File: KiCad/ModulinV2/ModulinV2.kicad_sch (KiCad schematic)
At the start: 13 parts, among them IC1 TL074HIDR, J1 NRJ4HF-1

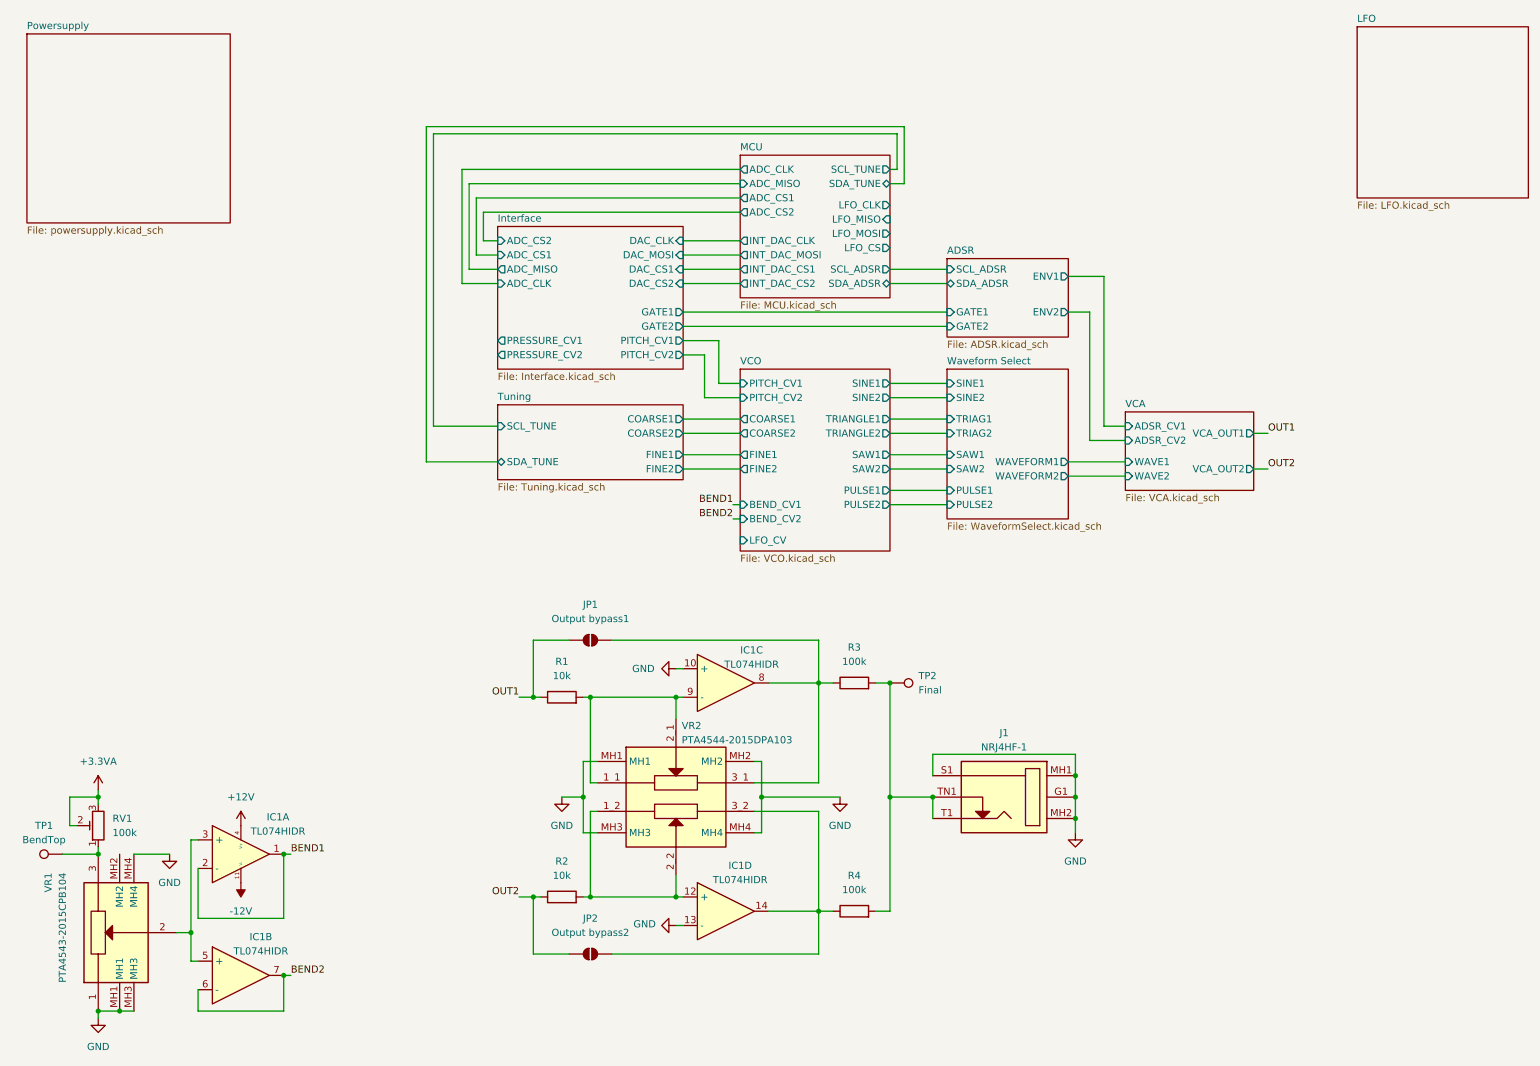
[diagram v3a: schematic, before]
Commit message: Made LFO and VCF schematics in addition to making a better reference voltage supply
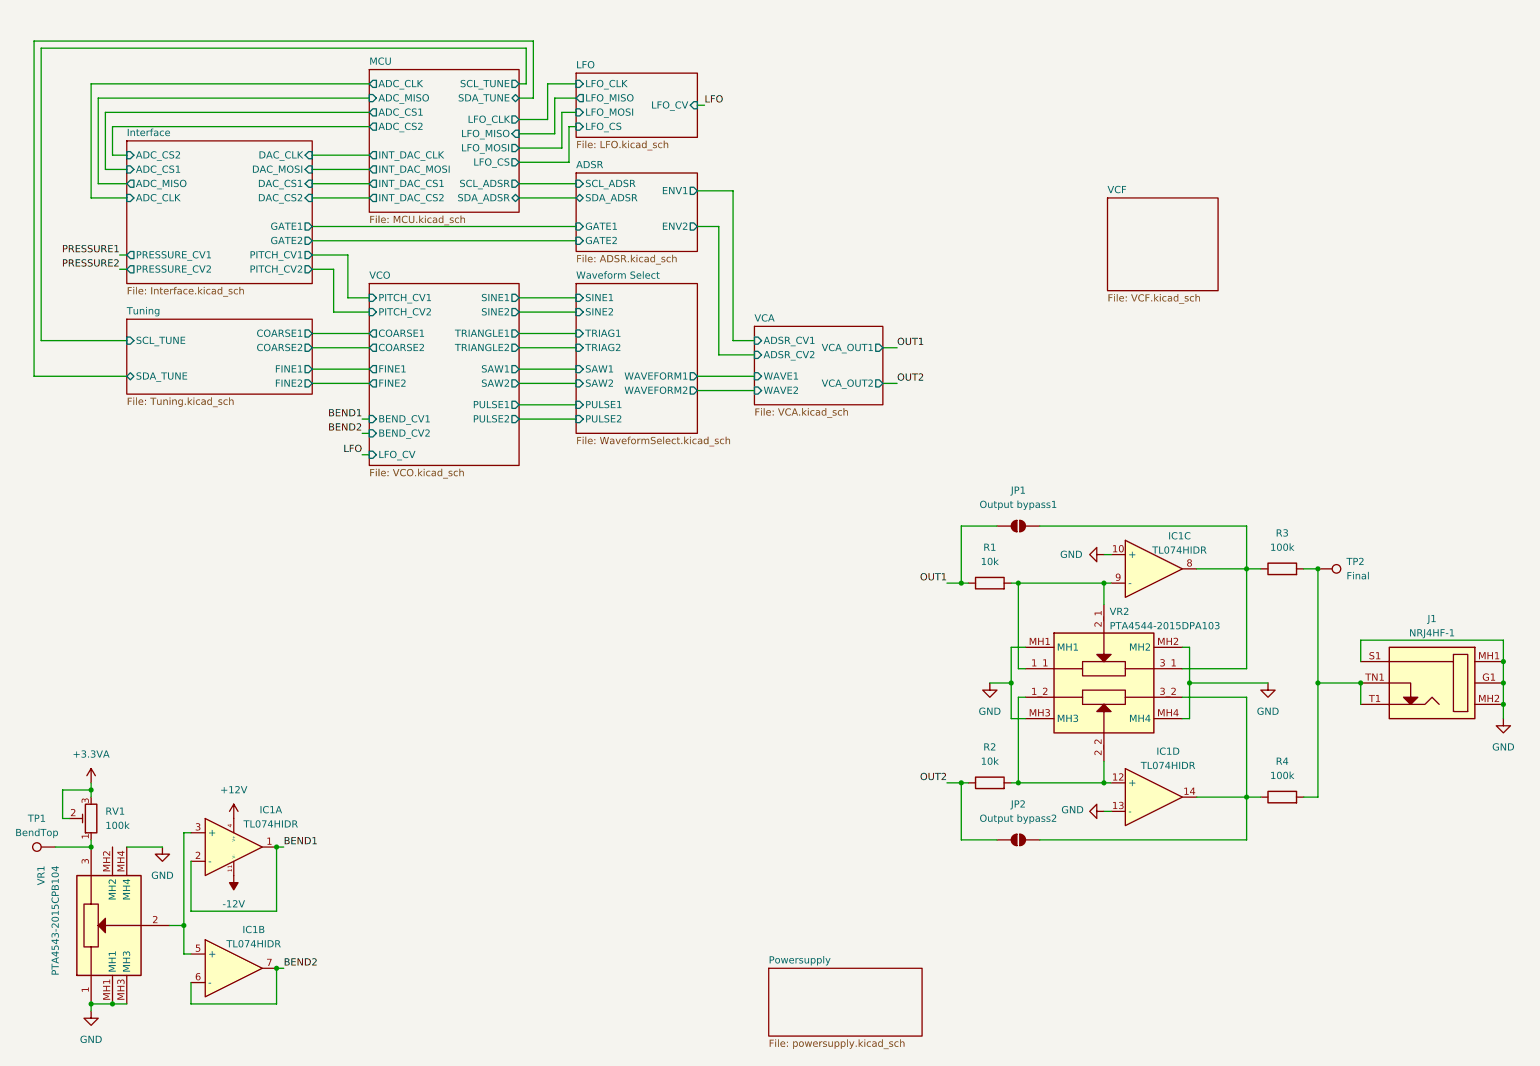
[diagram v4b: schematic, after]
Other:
- added sheet VCF (VCF.kicad_sch)
- sheet LFO ports: added LFO_CLK, LFO_CS, LFO_CV, LFO_MISO, LFO_MOSI; removed none
- moved on the sheet: IC1A, IC1B, IC1C, IC1D, J1, JP1, JP2, R1, R2, R3, R4, RV1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

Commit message: Finished Schematic, started on PCB
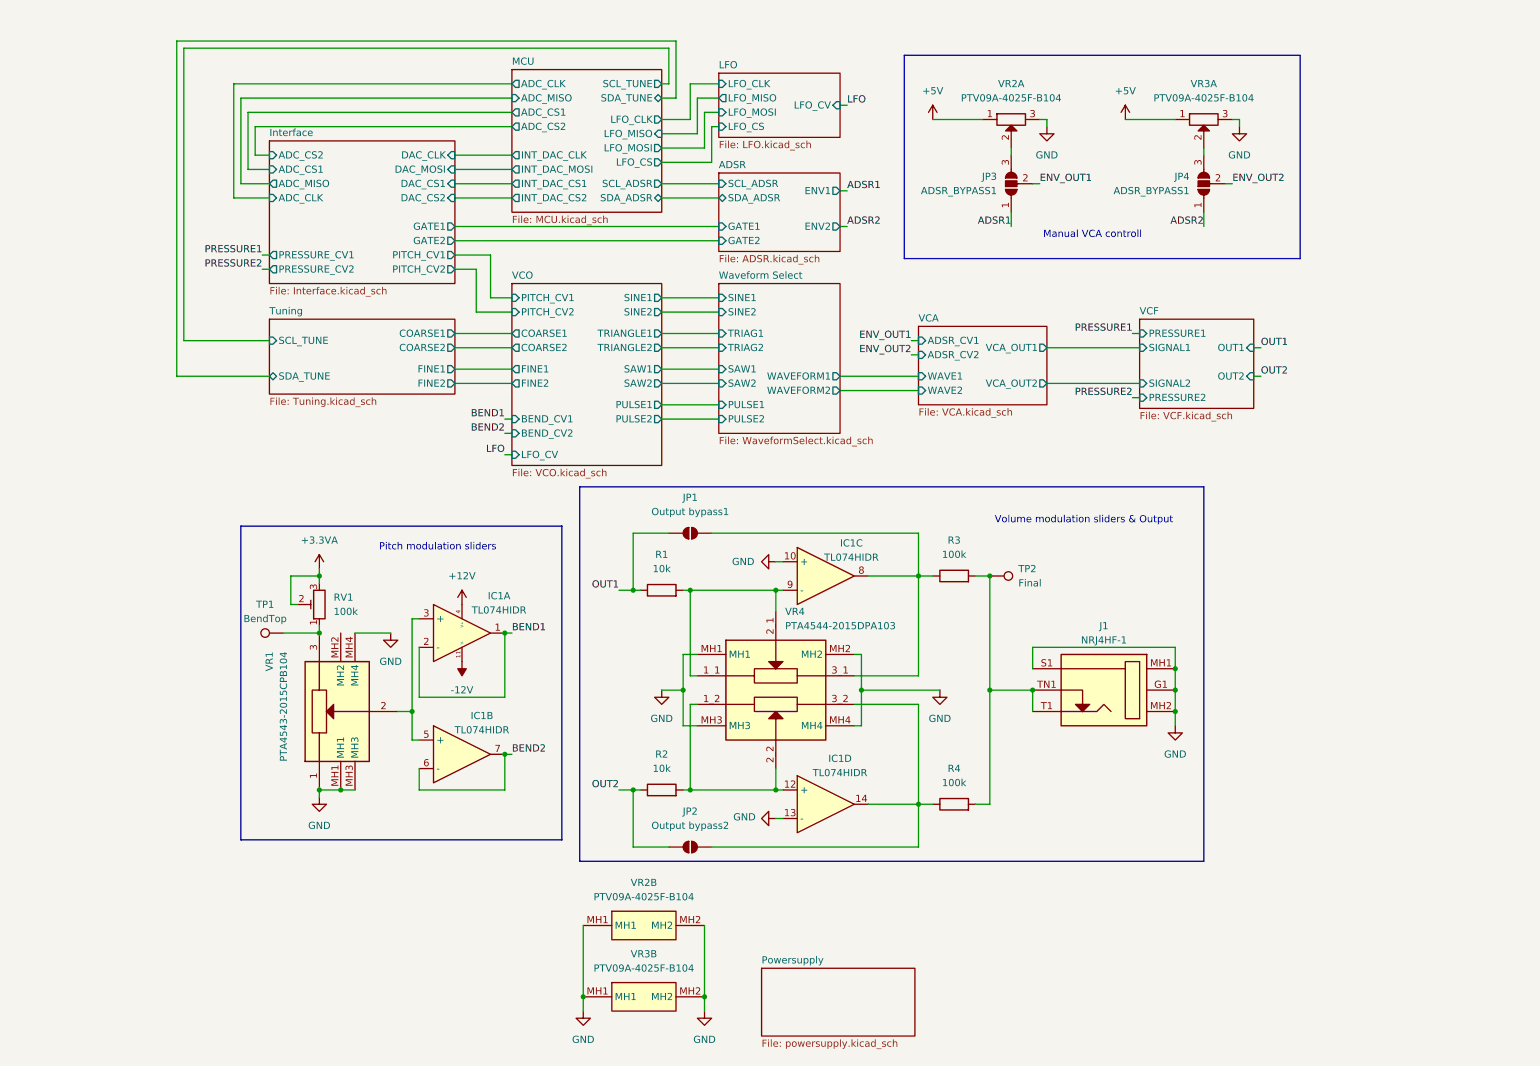
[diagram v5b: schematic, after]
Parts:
- removed VR2: PTA4544-2015DPA103, SamacSys_Parts:PTA45442015DPA103, symbol SamacSys_Parts:PTA4544-2015DPA103
- added JP3, JP4: ADSR_BYPASS1, Jumper:SolderJumper-3_P2.0mm_Open_TrianglePad1.0x1.5mm, symbol Jumper:SolderJumper_3_Open
- added VR2, VR3: PTV09A-4025F-B104, SamacSys_Parts:PTV09A4025FB104, symbol SamacSys_Parts:PTV09A-4025F-B104
- added VR4: PTA4544-2015DPA103, symbol SamacSys_Parts:PTA4544-2015DPA103
- R1, R2: footprint (none) -> Resistor_SMD:R_0603_1608Metric_Pad0.98x0.95mm_HandSolder
- R3, R4: footprint (none) -> Resistor_SMD:R_1206_3216Metric_Pad1.30x1.75mm_HandSolder
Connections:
- net GND: now also VR2.3, VR2.MH1, VR2.MH2, VR3.3, VR3.MH1, VR3.MH2, VR4.MH1, VR4.MH2, VR4.MH3, VR4.MH4
- net at IC1.12 (+), R2.2: now also VR4.1_2, VR4.2_2
- net at IC1.9 (-), R1.2: now also VR4.1_1, VR4.2_1
- net at IC1.8, JP1.2 (B), R3.1: now also VR4.3_1
- net at IC1.14, JP2.2 (B), R4.1: now also VR4.3_2
- new net: JP4.3 (B), VR3.2
- new net: JP3.3 (B), VR2.2
- new net +5V: VR2.1, VR3.1
- new net ADSR1: JP3.1 (A)
- new net ADSR2: JP4.1 (A)
- new net ENV_OUT1: JP3.2 (C)
- new net ENV_OUT2: JP4.2 (C)
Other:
- sheet VCF ports: added OUT1, OUT2, PRESSURE1, PRESSURE2, SIGNAL1, SIGNAL2; removed none
- note added: "Manual VCA controll"
- note added: "Pitch modulation sliders"
- note added: "Volume modulation sliders & Output"
- moved on the sheet: IC1A, IC1B, IC1C, IC1D, J1, JP1, JP2, R1, R2, R3, R4, RV1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

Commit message: Finished Schematic, started on PCB
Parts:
- VR4: footprint (none) -> SamacSys_Parts:PTA45442015DPA103
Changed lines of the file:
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@@
 			)
 		)
-		(property "Footprint" ""
+		(property "Footprint" "SamacSys_Parts:PTA45442015DPA103"
 			(at 139.7 121.92 0)
 			(effects

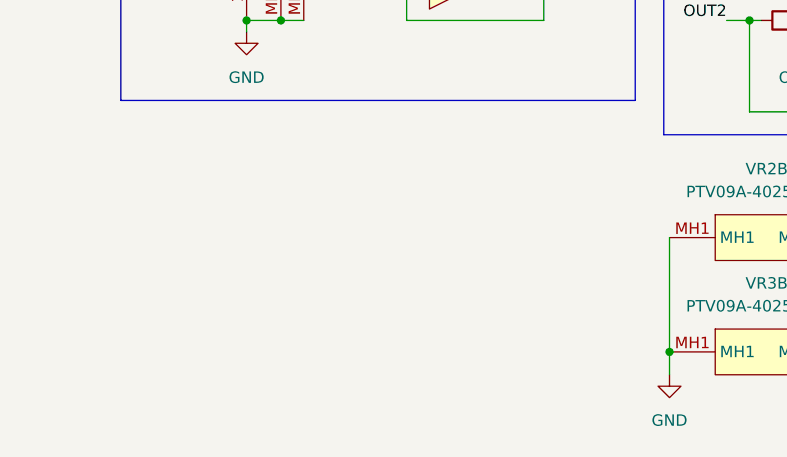
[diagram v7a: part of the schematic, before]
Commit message: Completed tuning & mod wheel layouts
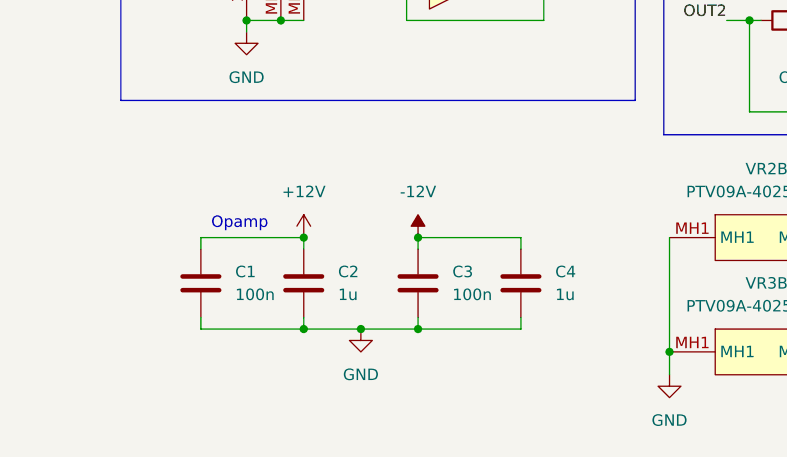
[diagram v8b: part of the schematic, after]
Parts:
- added C1, C3: 100n, Capacitor_SMD:C_0603_1608Metric_Pad1.08x0.95mm_HandSolder, symbol Device:C
- added C2, C4: 1u, Capacitor_SMD:C_0603_1608Metric_Pad1.08x0.95mm_HandSolder, symbol Device:C
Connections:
- net +12V: now also C1.2, C2.2
- net -12V: now also C3.2, C4.2
- net GND: now also C1.1, C2.1, C3.1, C4.1
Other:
- note added: "Opamp"
